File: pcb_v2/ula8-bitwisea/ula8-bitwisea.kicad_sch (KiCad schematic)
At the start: 11 parts, among them J1 ula8a, U1 74LS32, U2 74LS32, U3 74LS244

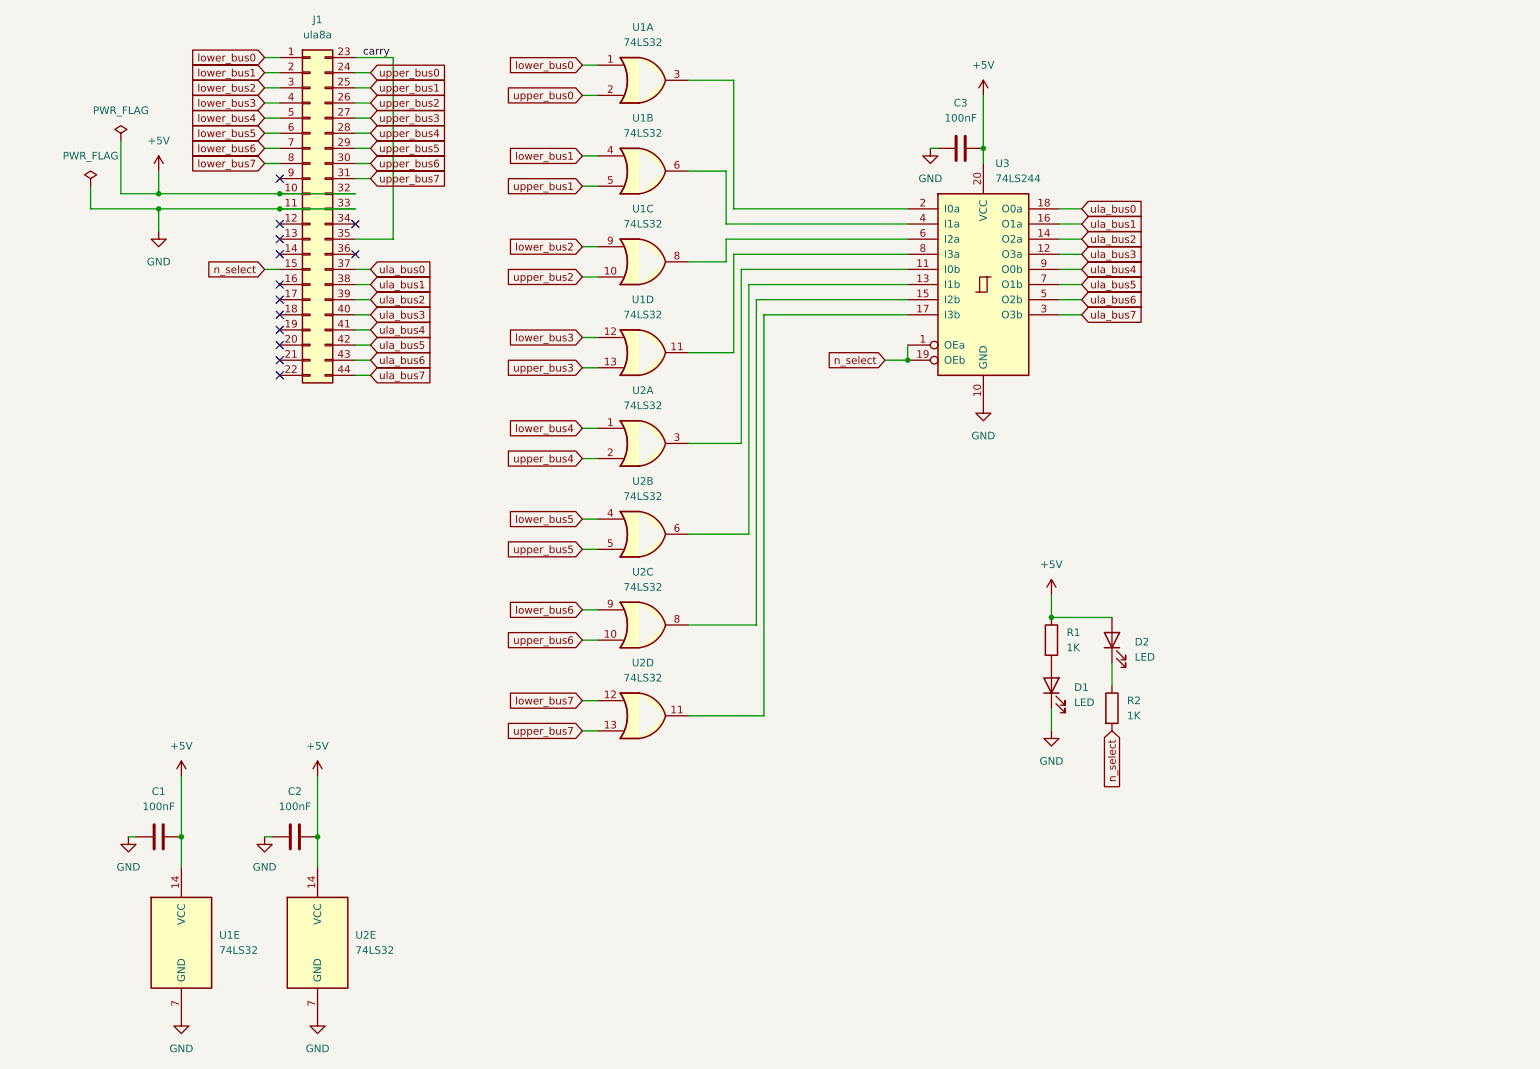
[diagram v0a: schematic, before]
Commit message: alimentação movida para as extremidades do conector
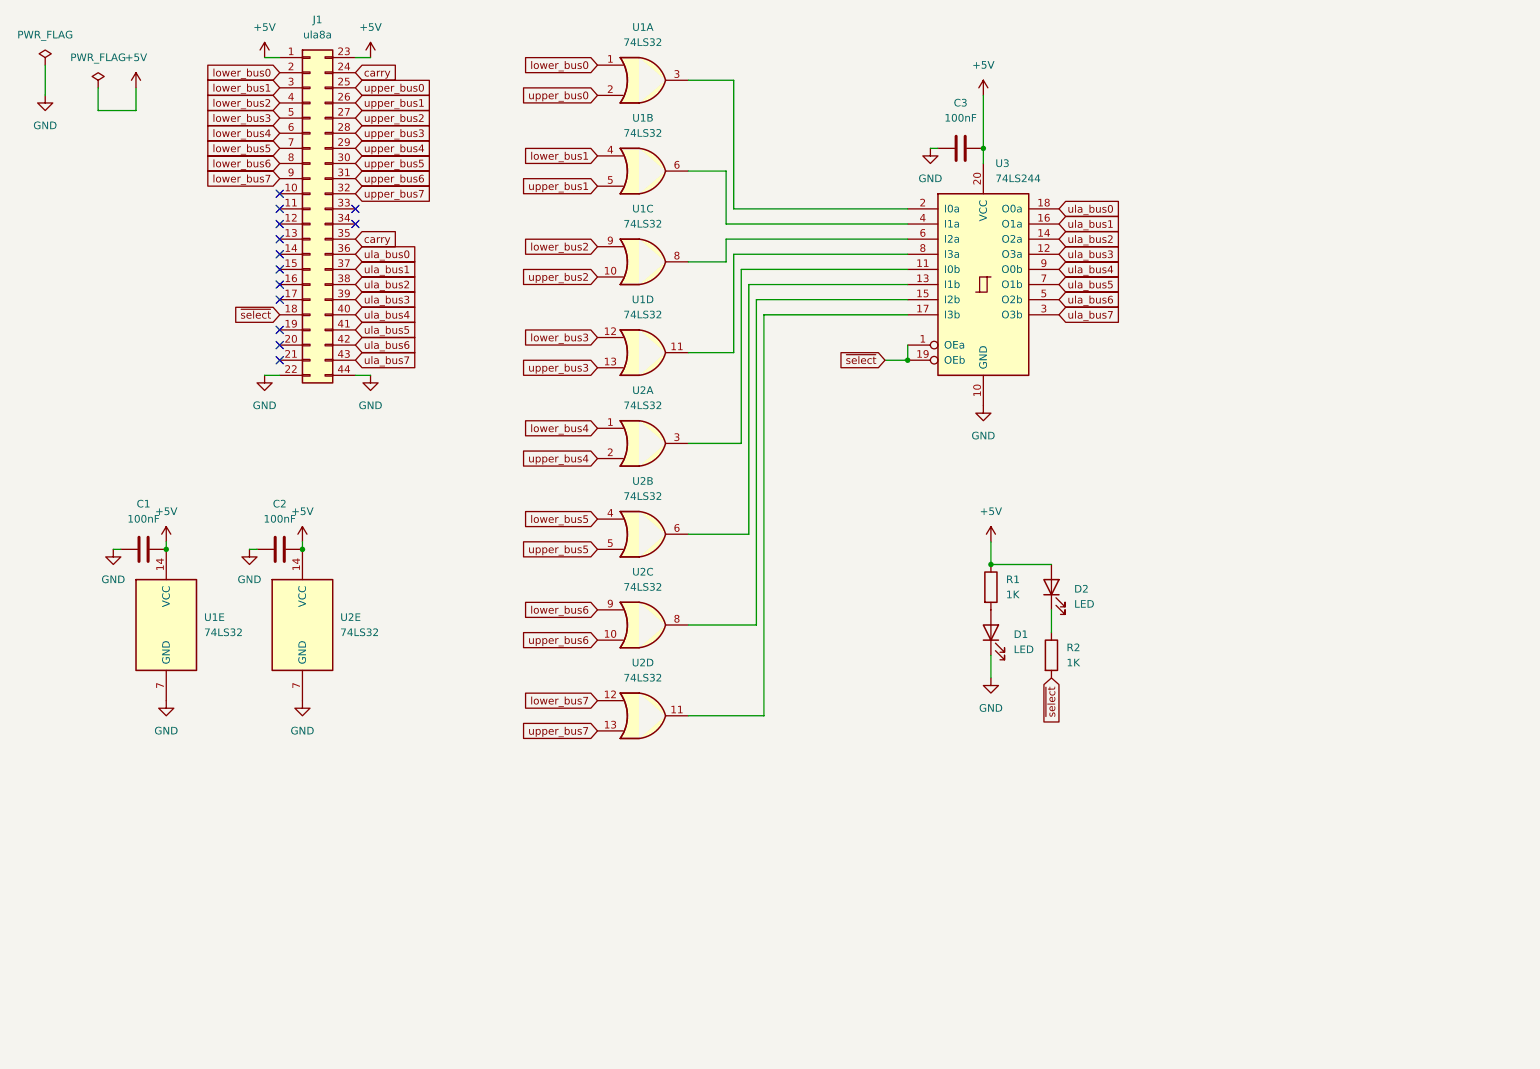
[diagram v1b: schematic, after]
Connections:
- net +5V: now also J1.1 (Pin_1), J1.23 (Pin_23); no longer J1.10 (Pin_10), J1.32 (Pin_32)
- net GND: now also J1.22 (Pin_22), J1.44 (Pin_44); no longer J1.11 (Pin_11), J1.33 (Pin_33)
- net carry: now also J1.24 (Pin_24); no longer J1.23 (Pin_23)
- net lower_bus0: now also J1.2 (Pin_2); no longer J1.1 (Pin_1)
- net lower_bus1: now also J1.3 (Pin_3); no longer J1.2 (Pin_2)
- net lower_bus2: now also J1.4 (Pin_4); no longer J1.3 (Pin_3)
- net lower_bus3: now also J1.5 (Pin_5); no longer J1.4 (Pin_4)
- net lower_bus4: now also J1.6 (Pin_6); no longer J1.5 (Pin_5)
- net lower_bus5: now also J1.7 (Pin_7); no longer J1.6 (Pin_6)
- net lower_bus6: now also J1.8 (Pin_8); no longer J1.7 (Pin_7)
- net lower_bus7: now also J1.9 (Pin_9); no longer J1.8 (Pin_8)
- net ula_bus0: now also J1.36 (Pin_36); no longer J1.37 (Pin_37)
- net ula_bus1: now also J1.37 (Pin_37); no longer J1.38 (Pin_38)
- net ula_bus2: now also J1.38 (Pin_38); no longer J1.39 (Pin_39)
- net ula_bus3: now also J1.39 (Pin_39); no longer J1.40 (Pin_40)
- net ula_bus4: now also J1.40 (Pin_40); no longer J1.41 (Pin_41)
- net ula_bus5: now also J1.41 (Pin_41); no longer J1.42 (Pin_42)
- net ula_bus6: now also J1.42 (Pin_42); no longer J1.43 (Pin_43)
- net ula_bus7: now also J1.43 (Pin_43); no longer J1.44 (Pin_44)
- net upper_bus0: now also J1.25 (Pin_25); no longer J1.24 (Pin_24)
- net upper_bus1: now also J1.26 (Pin_26); no longer J1.25 (Pin_25)
- net upper_bus2: now also J1.27 (Pin_27); no longer J1.26 (Pin_26)
- net upper_bus3: now also J1.28 (Pin_28); no longer J1.27 (Pin_27)
- net upper_bus4: now also J1.29 (Pin_29); no longer J1.28 (Pin_28)
- net upper_bus5: now also J1.30 (Pin_30); no longer J1.29 (Pin_29)
- net upper_bus6: now also J1.31 (Pin_31); no longer J1.30 (Pin_30)
- net upper_bus7: now also J1.32 (Pin_32); no longer J1.31 (Pin_31)
- net ~{select}: now reaches J1.18 (Pin_18)
- net ~{select}: now also R2.2, U3.1 (OEa), U3.19 (OEb)
- removed net n_select: J1.15 (Pin_15), R2.2, U3.1 (OEa), U3.19 (OEb)
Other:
- moved on the sheet: C1, C2, D1, D2, R1, R2, U1E, U2E

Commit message: deslocando alimentação para as estremidades do conector; carry out em três estados (ativo apenas quando select)
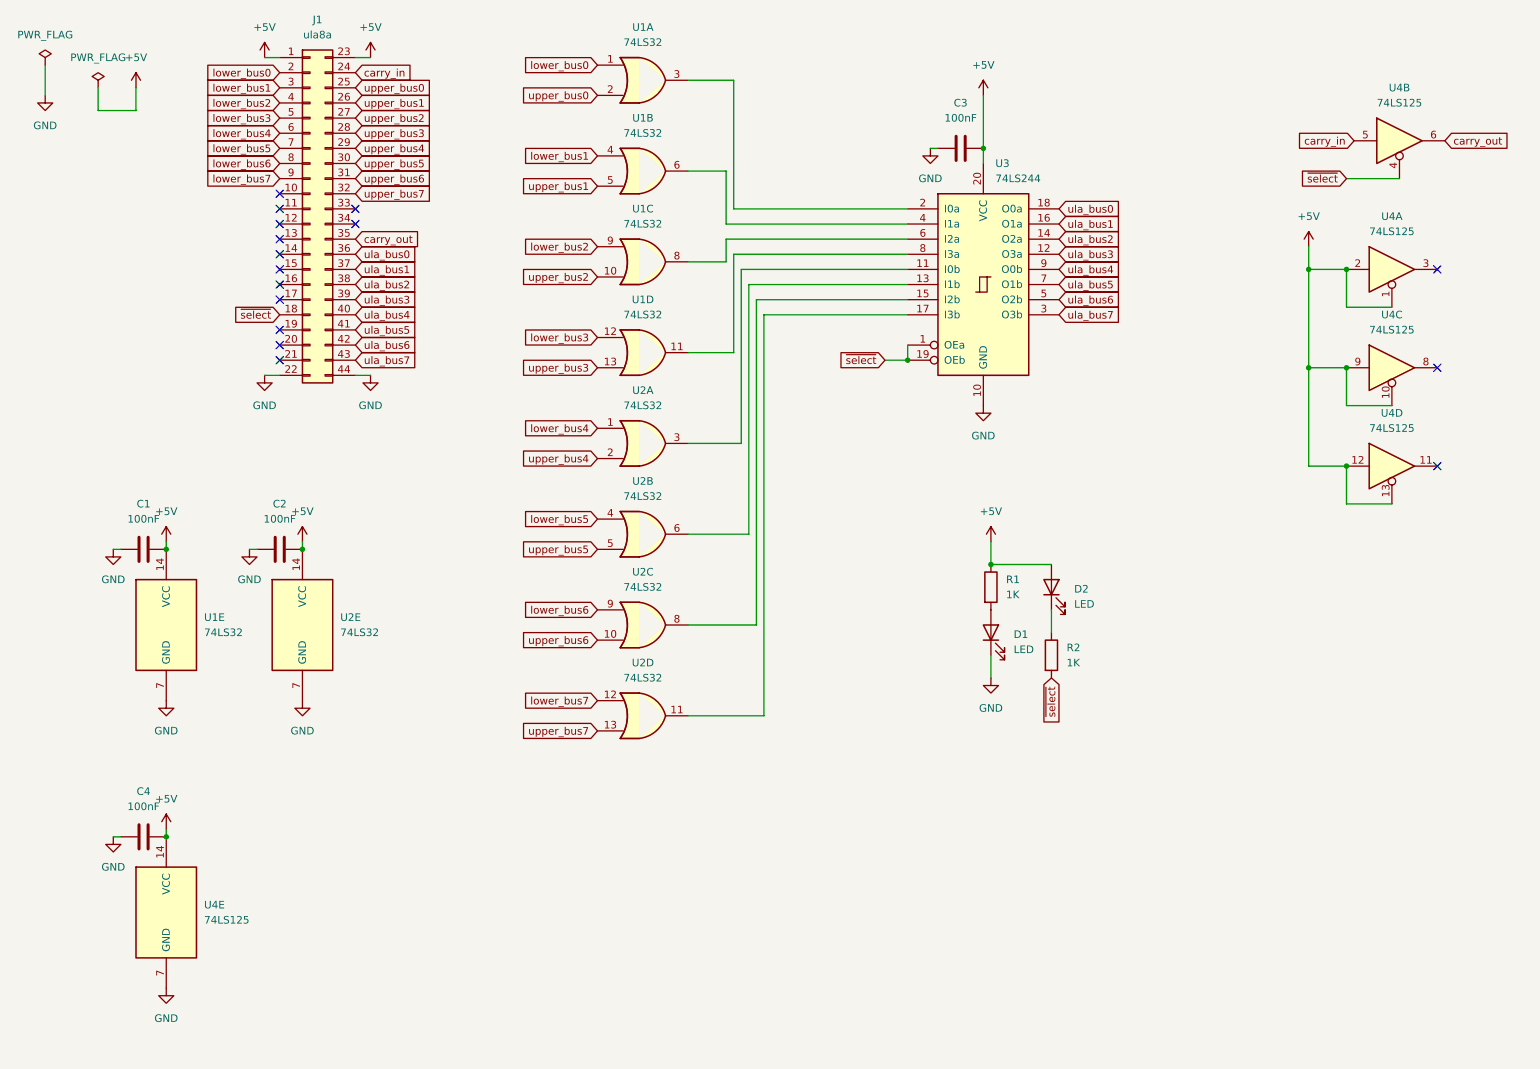
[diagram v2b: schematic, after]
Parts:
- added C4: 100nF, Capacitor_THT:C_Disc_D5.1mm_W3.2mm_P5.00mm, symbol Device:C
- added U4: 74LS125, Package_DIP:DIP-14_W7.62mm, symbol 74xx:74LS125
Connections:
- net +5V: now also C4.2, U4.1, U4.10, U4.12, U4.13, U4.14 (VCC), U4.2, U4.9
- net GND: now also C4.1, U4.7 (GND)
- net ~{select}: now also U4.4
- net carry renamed carry_in
- net carry_in: now also U4.5; no longer J1.35 (Pin_35)
- new net carry_out: J1.35 (Pin_35), U4.6
- no-connect marks 13 -> 16
